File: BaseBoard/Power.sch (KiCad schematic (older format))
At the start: 38 parts, among them J14 Conn_01x02_Female, J15 Conn_01x02_Female, J16 Conn_01x02_Female, J21 Conn_01x02_Female, J22 USB_C_Receptacle_USB2.0, J5 Barrel_Jack_Switch, K1 G5LE-1, U1 CH224K, U2 SY6912, U3 XL4005

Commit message: v2提交
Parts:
- removed JP1: SolderJumper_3_Open, Jumper:SolderJumper-3_P1.3mm_Open_Pad1.0x1.5mm_NumberLabels, symbol Jumper:SolderJumper_3_Open
- removed U2: SY6912, Package_SO:HSOP-8-1EP_3.9x4.9mm_P1.27mm_EP2.41x3.1mm_ThermalVias, symbol BaseBoard-rescue:SY6912-custom
- added C29: 10uF, Capacitor_SMD:C_0603_1608Metric, symbol Device:C_Small
- added C30: 100pF, Capacitor_SMD:C_0402_1005Metric, symbol Device:C_Small
- added C31, C33, C34: 1uF, Capacitor_SMD:C_0402_1005Metric, symbol Device:C_Small
- added C32: 470uF, Capacitor_SMD:CP_Elec_10x10.5, symbol Device:C_Small
- added Q1: 9926A, Package_SO:SO-8_3.9x4.9mm_P1.27mm, symbol Transistor_FET:FDS9926A
- added R21: 1.6k, Resistor_SMD:R_0603_1608Metric, symbol Device:R_Small
- added R22: 95.3k, Resistor_SMD:R_0603_1608Metric, symbol Device:R_Small
- added R23: 910k, Resistor_SMD:R_0603_1608Metric, symbol Device:R_Small
- added R24: 1k, Resistor_SMD:R_0402_1005Metric, symbol Device:R_Small
- added R25: 0.02R, Resistor_SMD:R_2512_6332Metric, symbol Device:R_Small
- added R26: 0.05R/2W, Resistor_SMD:R_2512_6332Metric, symbol Device:R_Small
- added U2: CN3306, Package_SO:TSSOP-16_4.4x5mm_P0.65mm, symbol custom:CN3306
- added U7: XC6206PxxxMR, Package_TO_SOT_SMD:SOT-23, symbol Regulator_Linear:XC6206PxxxMR
- C1: value 10uF/X7R -> 100uF; footprint Capacitor_SMD:C_0805_2012Metric -> Capacitor_SMD:CP_Elec_6.3x7.7
- C10, C2, C7: footprint Capacitor_SMD:C_0805_2012Metric -> Capacitor_SMD:C_0402_1005Metric
- C3: value 470nF -> 22nF; footprint Capacitor_SMD:C_0805_2012Metric -> Capacitor_SMD:C_0402_1005Metric
- C4: value 10uF/X7R -> 470nF; footprint Capacitor_SMD:C_0805_2012Metric -> Capacitor_SMD:C_0402_1005Metric
- C5, C9: value 105 -> 1uF; footprint Capacitor_SMD:C_0805_2012Metric -> Capacitor_SMD:C_0402_1005Metric
- D3: value SS34 -> SS54; footprint Diode_SMD:D_SMA -> Diode_SMD:D_SMB
- K1: value G5LE-1 -> SRD-12V
- L1: value 2.2uH -> 4.7uH
- R1, R10, R4, R6, R7: footprint Resistor_SMD:R_0805_2012Metric -> Resistor_SMD:R_0402_1005Metric
- R11, R8, R9: footprint Resistor_SMD:R_0805_2012Metric -> Resistor_SMD:R_0603_1608Metric
- R2: value 25mR -> 820k; footprint Resistor_SMD:R_1206_3216Metric -> Resistor_SMD:R_0603_1608Metric
- R3: value 10k -> 95.3k; footprint Resistor_SMD:R_0805_2012Metric -> Resistor_SMD:R_0603_1608Metric
- R5: value 56k -> 24k; footprint Resistor_SMD:R_0805_2012Metric -> Resistor_SMD:R_0402_1005Metric
- U1: footprint Custom:ESSOP10 -> Customv2:ESSOP10
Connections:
- net +5V: now also C33.1, U7.3 (VI)
- net +BATT: now also C31.1, R23.1, R26.1, U2.9 (BAT); no longer C1.1, R2.2
- net GND: now also C3.2, R3.2, C29.2, C30.2, C31.2, C32.2, C33.2, C34.2, R22.2, R25.2, U2.14 (GND), U2.15 (GND), U2.5 (~SHDN), U7.1 (GND); no longer C3.1, D2.1 (K), R4.1
- net VBUS: now also C1.1, L1.1, R2.1, R4.1, R7.1, U2.10 (VIN); no longer D3.2 (A)
- net at D1.1 (K): now also U2.6 (~CHRG); no longer D2.2 (A)
- net at R3.1: now also R2.2, U2.3 (MPPT); no longer R4.2
- net RS: no longer names the net of L1.2
- net RS: now also D3.2 (A), Q1.7 (D1), Q1.8 (D1); no longer R2.1
- removed net VCHARGE: C4.1, D3.1 (K), R3.2, R7.1
- new net: R22.1, R23.2, U2.1 (FB)
- new net: C29.1, U2.11 (VCC), U2.12 (VCC)
- new net: Q1.2 (G1), U2.13 (DRV)
- new net: C30.1, R24.2, U2.16 (ISW)
- new net: C3.1, R21.1, U2.2 (COMP)
- new net: D2.1 (K), U2.7 (~DONE)
- new net: C32.1, D3.1 (K), R26.2, U2.8 (CSP)
- new net: D2.2 (A), R4.2
- new net: C4.1, R21.2
- new net: Q1.1 (S1), R24.1, R25.1
- new net +3V3: C34.1, U7.2 (VO)
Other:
- note removed: "C(nF) = 0.02 * T(s)"
- note removed: "CEL"
- note removed: "I = 25/R"
- moved on the sheet: C10, D1, D2, D3, J14, J15, J16, J5, K1, L1, R10, R11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

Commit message: Modify some footprints.
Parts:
- C4: footprint Capacitor_SMD:C_0402_1005Metric -> Capacitor_SMD:C_0603_1608Metric
- D3, D4: footprint Diode_SMD:D_SMB -> Diode_SMD:D_SMA
- U2: symbol custom:CN3306 -> BaseBoard-rescue:CN3306-custom
- U3: symbol custom:XL4005 -> BaseBoard-rescue:XL4005-custom
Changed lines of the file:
@@
 $EndComp
 $Comp
-L custom:XL4005 U3
+L BaseBoard-rescue:XL4005-custom U3
 U 1 1 612938CB
 P 2850 6700
@@
 F 0 "D4" H 3500 6417 50  0000 C CNN
 F 1 "SS54" H 3500 6326 50  0000 C CNN
-F 2 "Diode_SMD:D_SMB" H 3500 6200 50  0001 C CNN
+F 2 "Diode_SMD:D_SMA" H 3500 6200 50  0001 C CNN
 F 3 "~" H 3500 6200 50  0001 C CNN
 	1    3500 6200
@@
 F 0 "D3" H 10050 983 50  0000 C CNN
 F 1 "SS54" H 10050 1074 50  0000 C CNN
-F 2 "Diode_SMD:D_SMB" H 10050 1200 50  0001 C CNN
+F 2 "Diode_SMD:D_SMA" H 10050 1200 50  0001 C CNN
 F 3 "~" H 10050 1200 50  0001 C CNN
 	1    10050 1200
@@
 $EndComp
 $Comp
-L custom:CN3306 U2
+L BaseBoard-rescue:CN3306-custom U2
 U 1 1 611457D3
 P 8800 2050
@@
 F 0 "C4" H 8092 2746 50  0000 L CNN
 F 1 "470nF" H 8092 2655 50  0000 L CNN
-F 2 "Capacitor_SMD:C_0402_1005Metric" H 8000 2700 50  0001 C CNN
+F 2 "Capacitor_SMD:C_0603_1608Metric" H 8000 2700 50  0001 C CNN
 F 3 "~" H 8000 2700 50  0001 C CNN
 	1    8000 2700

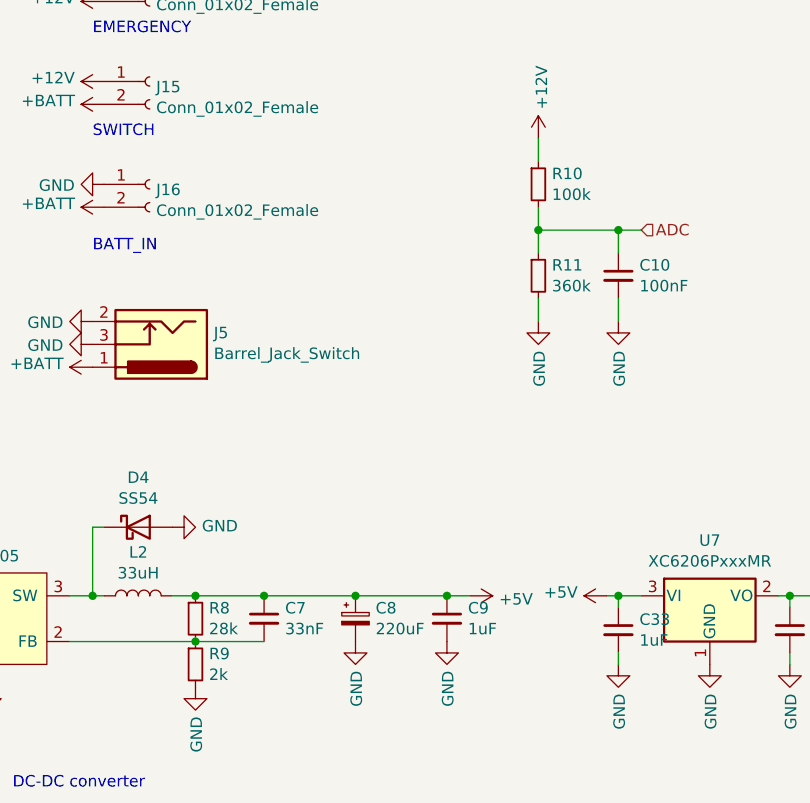
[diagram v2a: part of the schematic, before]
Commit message: 修正两处电阻阻值不正确的问题
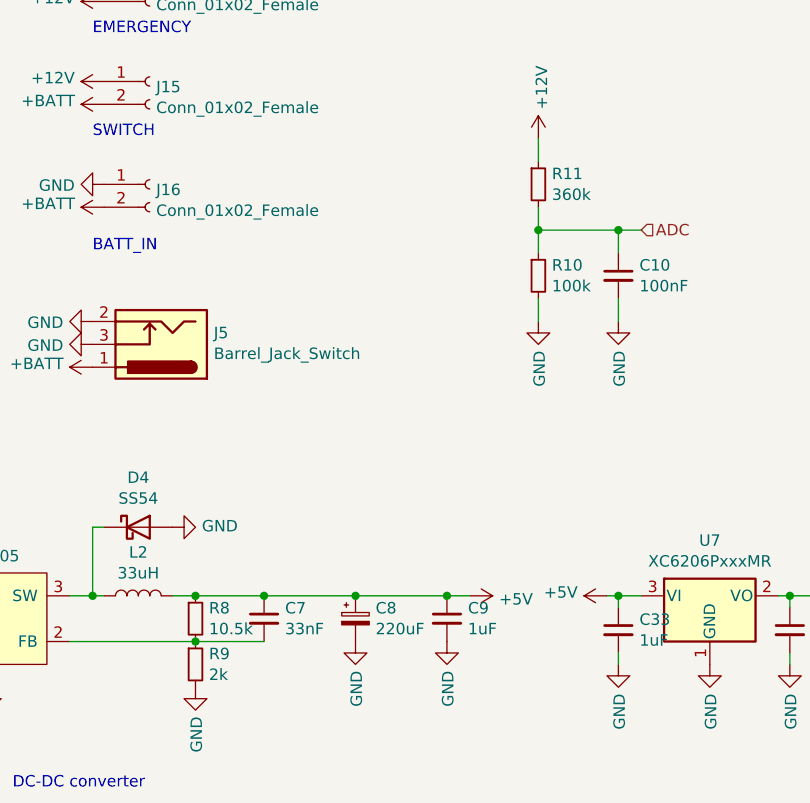
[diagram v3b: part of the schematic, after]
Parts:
- R8: value 28k -> 10.5k
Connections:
- net +12V: now also R11.1; no longer R10.1
- net ADC: now also R10.1, R11.2; no longer R10.2, R11.1
- net GND: now also R10.2; no longer R11.2
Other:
- moved on the sheet: R10, R11
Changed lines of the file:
@@
-$EndComp
-$Comp
-L BaseBoard-rescue:USB_C_Receptacle_USB2.0-Connector J?
-U 1 1 6123F1A8
-P 7400 5300
-AR Path="/6123F1A8" Ref="J?"  Part="1"
-AR Path="/611CF83A/6123F1A8" Ref="J22"  Part="1"
-F 0 "J22" H 7507 6167 50  0000 C CNN
-F 1 "USB_C_Receptacle_USB2.0" H 7507 6076 50  0000 C CNN
-F 2 "Connector_USB:USB_C_Receptacle_HRO_TYPE-C-31-M-12" H 7550 5300 50  0001 C CNN
-F 3 "https://www.usb.org/sites/default/files/documents/usb_type-c.zip" H 7550 5300 50  0001 C CNN
-	1    7400 5300
-	1    0    0    -1
 $EndComp
 $Comp
@@
 P 3750 6600
 F 0 "R8" H 3809 6646 50  0000 L CNN
-F 1 "28k" H 3809 6555 50  0000 L CNN
+F 1 "10.5k" H 3809 6555 50  0000 L CNN
 F 2 "Resistor_SMD:R_0603_1608Metric" H 3750 6600 50  0001 C CNN
 F 3 "~" H 3750 6600 50  0001 C CNN
@@
 L Device:R_Small R11
 U 1 1 612C7569
+P 5250 4700
+F 0 "R11" H 5309 4746 50  0000 L CNN
+F 1 "360k" H 5309 4655 50  0000 L CNN
+F 2 "Resistor_SMD:R_0603_1608Metric" H 5250 4700 50  0001 C CNN
+F 3 "~" H 5250 4700 50  0001 C CNN
+	1    5250 4700
+	1    0    0    -1
+$EndComp
+$Comp
+L Device:R_Small R10
+U 1 1 612CC439
 P 5250 5100
-F 0 "R11" H 5309 5146 50  0000 L CNN
-F 1 "360k" H 5309 5055 50  0000 L CNN
-F 2 "Resistor_SMD:R_0603_1608Metric" H 5250 5100 50  0001 C CNN
+F 0 "R10" H 5309 5146 50  0000 L CNN
+F 1 "100k" H 5309 5055 50  0000 L CNN
+F 2 "Resistor_SMD:R_0402_1005Metric" H 5250 5100 50  0001 C CNN
 F 3 "~" H 5250 5100 50  0001 C CNN
 	1    5250 5100
-	1    0    0    -1
-$EndComp
-$Comp
-L Device:R_Small R10
-U 1 1 612CC439
-P 5250 4700
-F 0 "R10" H 5309 4746 50  0000 L CNN
-F 1 "100k" H 5309 4655 50  0000 L CNN
-F 2 "Resistor_SMD:R_0402_1005Metric" H 5250 4700 50  0001 C CNN
-F 3 "~" H 5250 4700 50  0001 C CNN
-	1    5250 4700
 	1    0    0    -1
 $EndComp
@@
 Wire Wire Line
 	6350 6750 6350 6800
+$Comp
+L BaseBoard-rescue:USB_C_Receptacle_USB2.0-Connector J?
+U 1 1 6123F1A8
+P 7400 5300
+AR Path="/6123F1A8" Ref="J?"  Part="1"
+AR Path="/611CF83A/6123F1A8" Ref="J22"  Part="1"
+F 0 "J22" H 7507 6167 50  0000 C CNN
+F 1 "USB_C_Receptacle_USB2.0" H 7507 6076 50  0000 C CNN
+F 2 "Connector_USB:USB_C_Receptacle_HRO_TYPE-C-31-M-12" H 7550 5300 50  0001 C CNN
+F 3 "https://www.usb.org/sites/default/files/documents/usb_type-c.zip" H 7550 5300 50  0001 C CNN
+	1    7400 5300
+	1    0    0    -1
+$EndComp
 $EndSCHEMATC
